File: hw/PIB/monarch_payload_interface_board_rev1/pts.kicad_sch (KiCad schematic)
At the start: 11 parts, among them U9 AD7124-8BCPZ-RL

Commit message: PCB updates
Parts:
- R32, R33, R34, R35, R36, R37, R38, R39: footprint Resistor_SMD:R_0402_1005Metric -> Resistor_SMD:R_0603_1608Metric

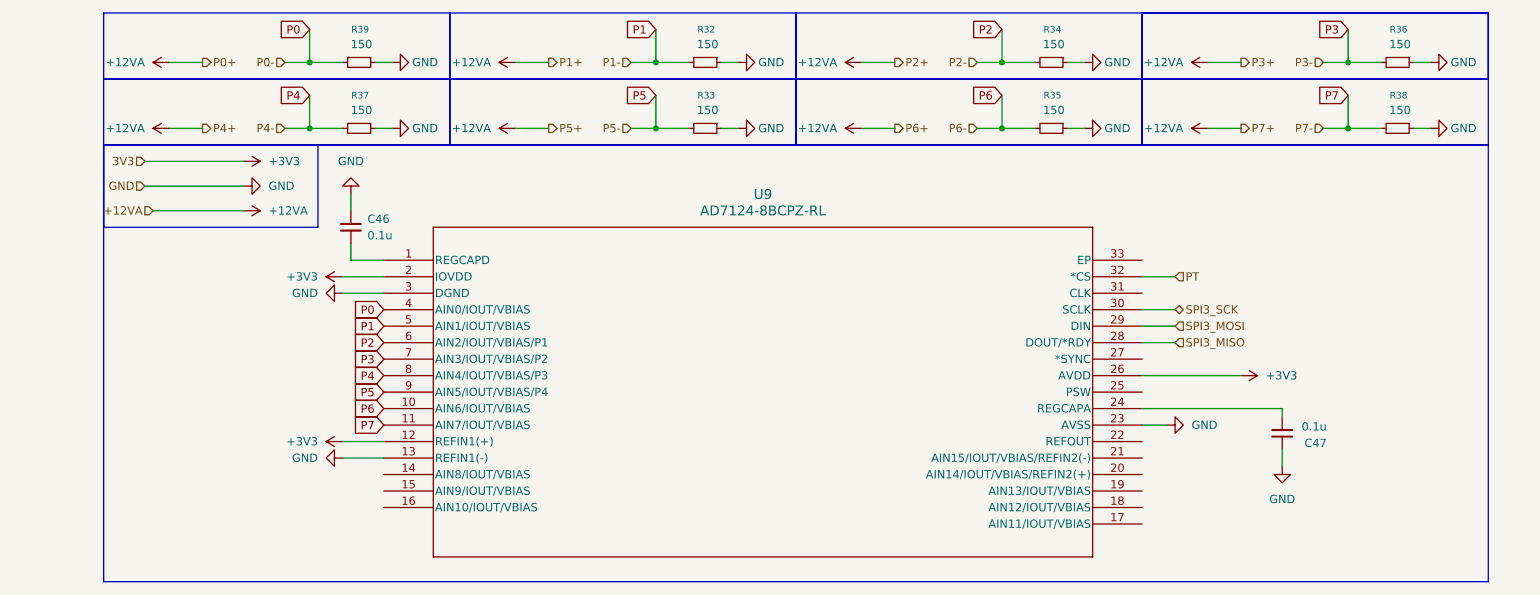
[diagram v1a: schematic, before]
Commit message: PIB layout update
done pending Ben O approval
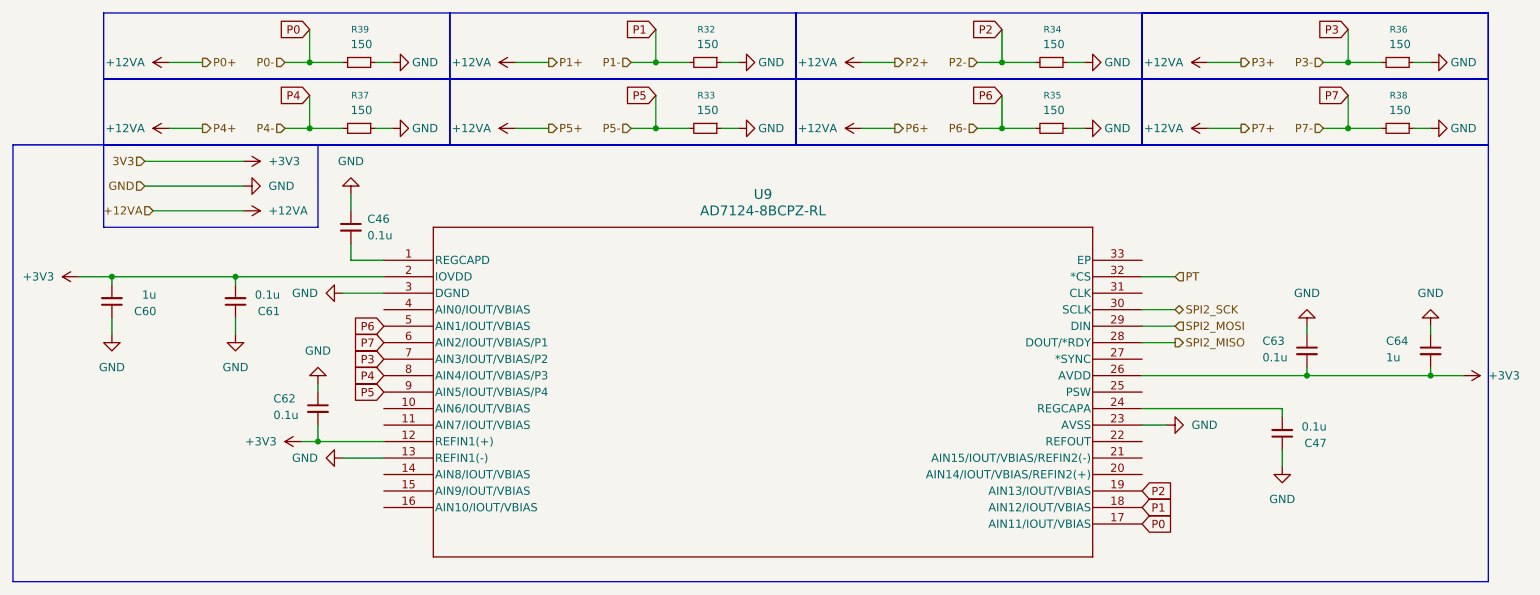
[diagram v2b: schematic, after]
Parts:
- added C60, C64: 1u, Capacitor_SMD:C_0603_1608Metric, symbol Device:C_Small
- added C61, C62, C63: 0.1u, Capacitor_SMD:C_0603_1608Metric, symbol Device:C_Small
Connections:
- net +3V3: now also C60.2, C61.2, C62.2, C63.2, C64.2
- net GND: now also C60.1, C61.1, C62.1, C63.1, C64.1
- net P0: now also U9.17 (AIN11/IOUT/VBIAS); no longer U9.4 (AIN0/IOUT/VBIAS)
- net P1: now also U9.18 (AIN12/IOUT/VBIAS); no longer U9.5 (AIN1/IOUT/VBIAS)
- net P2: now also U9.19 (AIN13/IOUT/VBIAS); no longer U9.6 (AIN2/IOUT/VBIAS/P1)
- net P6: now also U9.5 (AIN1/IOUT/VBIAS); no longer U9.10 (AIN6/IOUT/VBIAS)
- net P7: now also U9.6 (AIN2/IOUT/VBIAS/P1); no longer U9.11 (AIN7/IOUT/VBIAS)
- net SPI3_MISO renamed SPI2_MISO
- net SPI3_MOSI renamed SPI2_MOSI
- net SPI3_SCK renamed SPI2_SCK
